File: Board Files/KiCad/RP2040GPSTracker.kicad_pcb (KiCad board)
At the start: 2 copper layers, 99.6 x 53 mm, 116 parts, among them J1 BOOTSEL, J10 GNSS, J2 RESET, J3 DEBUG, J4 BT(LE), J5 GSM, J6 USBC_CHARGE, J7 USBC_PROG, J8 2822541-1, J9 BATTERY, U1 W25Q128JVS, U10 LM66200DRLR, U2 SIM868, U3 RP2040, U4 SN74LVC1G66DRYR, U5 LM66200DRLR, U6 MP2624GL, U7 NCP1117LPST33T3G, U8 SAFFB1G56KB0F5F, Y1 Crystal

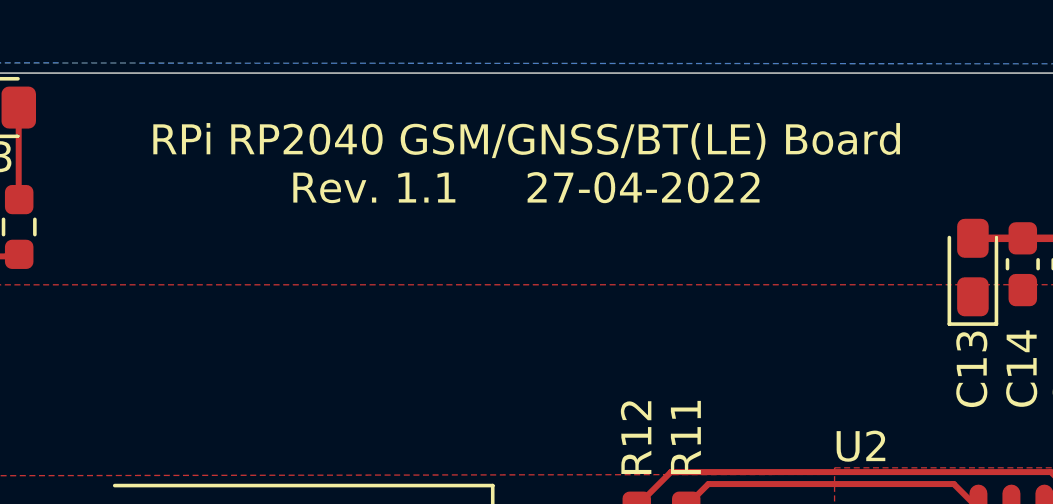
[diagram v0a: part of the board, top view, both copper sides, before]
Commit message: Updated type in Board Files
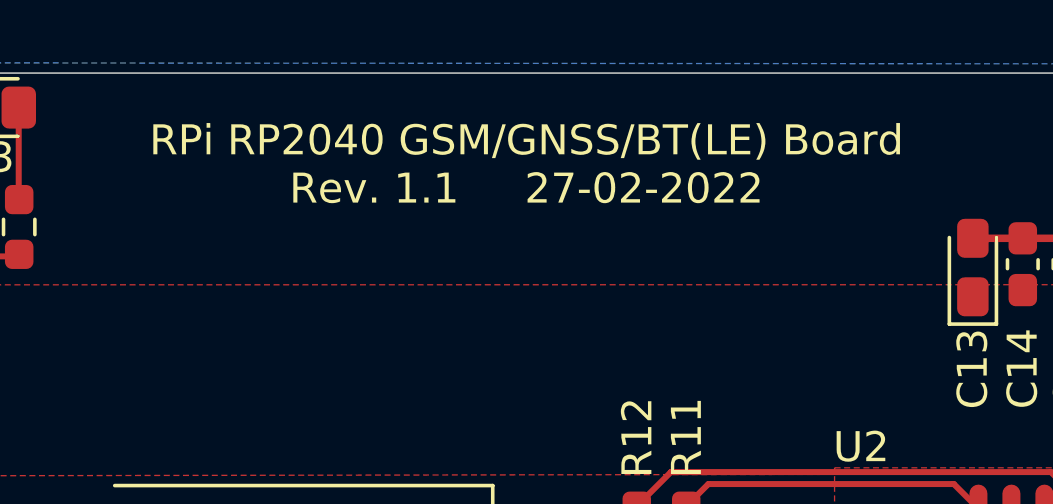
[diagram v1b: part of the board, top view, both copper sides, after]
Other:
- board text added: "RPi RP2040 GSM/GNSS/BT(LE) Board Rev. 1.1 27-02-2022"
- board text removed: "RPi RP2040 GSM/GNSS/BT(LE) Board Rev. 1.1 27-04-2022"
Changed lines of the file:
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@@
     (effects (font (size 1.5 1.5) (thickness 0.3)))
   )
-  (gr_text "RPi RP2040 GSM/GNSS/BT(LE) Board\nRev. 1.1     27-04-2022" (at 131.2852 6.9146) (layer "F.SilkS")
+  (gr_text "RPi RP2040 GSM/GNSS/BT(LE) Board\nRev. 1.1     27-02-2022" (at 131.2852 6.9146) (layer "F.SilkS")
     (effects (font (size 1 1) (thickness 0.2)))
   )

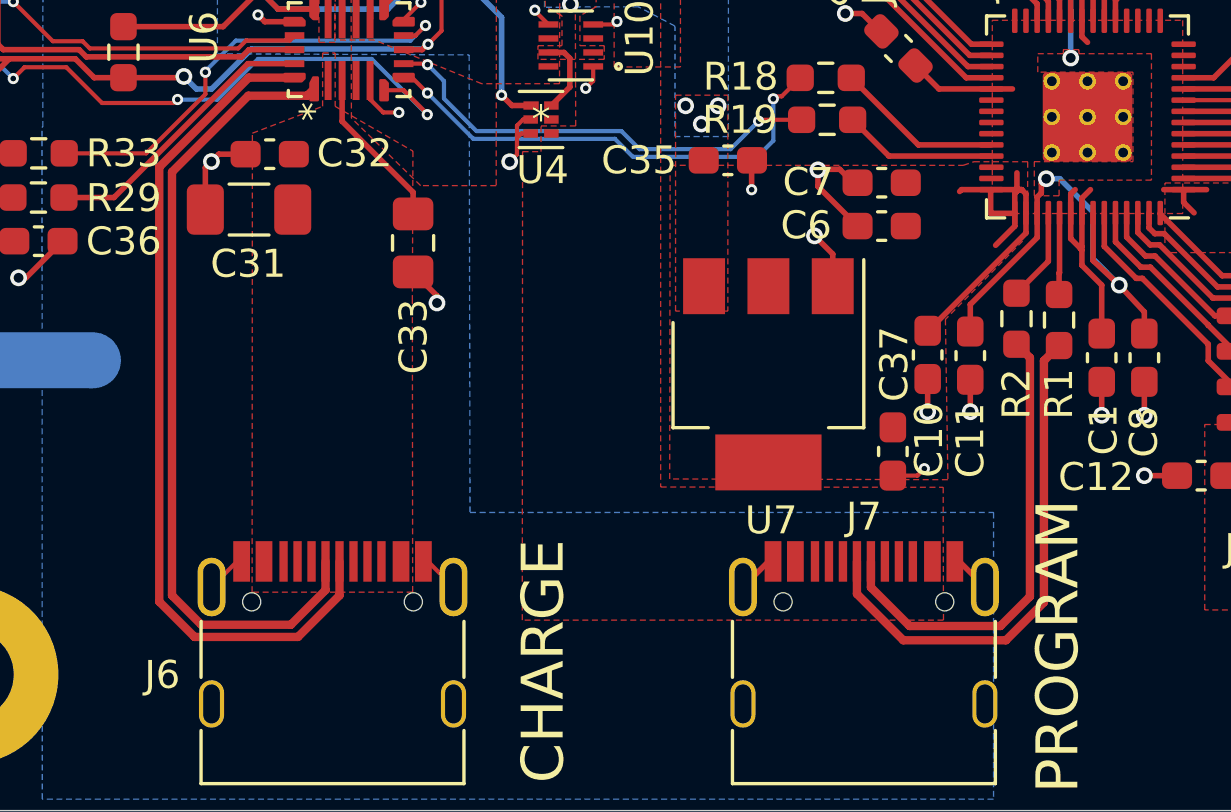
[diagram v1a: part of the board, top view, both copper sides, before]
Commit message: Updated USB trace differential routing
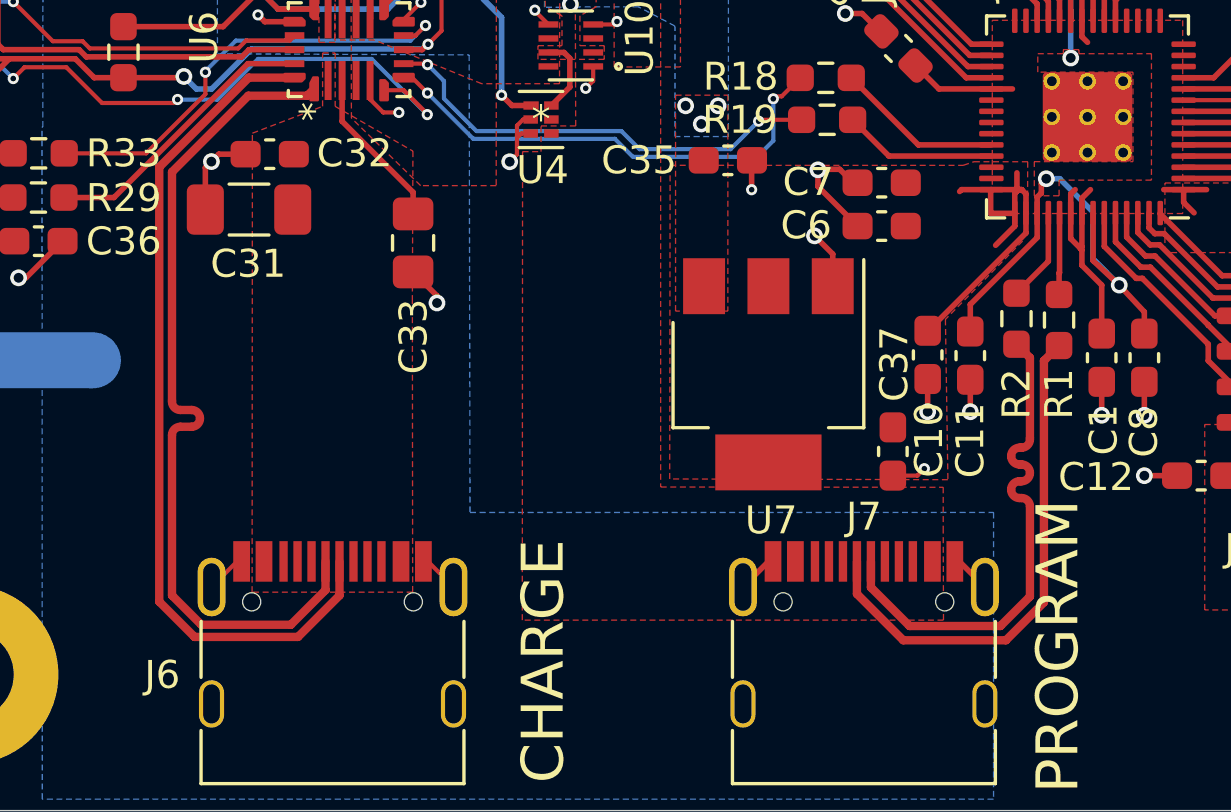
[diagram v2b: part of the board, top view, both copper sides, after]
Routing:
- net /USB_D-: track 16.8 -> 18.4 mm
- net /BCM_D+: track 28.9 -> 30.4 mm
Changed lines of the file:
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@@
 (kicad_pcb (version 20211014) (generator pcbnew)
   (general
-    (thickness 1.6)
+    (thickness 1)
   )
   (paper "A4")
@@
       (layer "F.Mask" (type "Top Solder Mask") (color "Black") (thickness 0.01))
       (layer "F.Cu" (type "copper") (thickness 0.035))
-      (layer "dielectric 1" (type "core") (thickness 1.51) (material "FR4") (epsilon_r 4.5) (loss_tangent 0.02))
+      (layer "dielectric 1" (type "core") (thickness 0.91) (material "FR4") (epsilon_r 4.5) (loss_tangent 0.02))
       (layer "B.Cu" (type "copper") (thickness 0.035))
       (layer "B.Mask" (type "Bottom Solder Mask") (color "Black") (thickness 0.01))
@@
   (segment (start 92.8852 27.3446) (end 94.0452 28.5046) (width 0.2) (layer "B.Cu") (net 33))
   (segment (start 86.053304 28.207704) (end 89.982096 28.207704) (width 0.2) (layer "B.Cu") (net 33))
-  (segment (start 113.435719 49.416911) (end 112.07803 50.7746) (width 0.3) (layer "F.Cu") (net 34))
-  (segment (start 113.9782 40.237) (end 113.43572 40.77948) (width 0.3) (layer "F.Cu") (net 34))
-  (segment (start 108.4072 50.7746) (end 106.75 49.1174) (width 0.3) (layer "F.Cu") (net 34))
-  (segment (start 112.07803 50.7746) (end 108.4072 50.7746) (width 0.3) (layer "F.Cu") (net 34))
-  (segment (start 113.43572 40.77948) (end 113.435719 49.416911) (width 0.3) (layer "F.Cu") (net 34))
-  (segment (start 106.75 49.1174) (end 106.75 47.955) (width 0.3) (layer "F.Cu") (net 34))
+  (segment (start 106.75 49.1174) (end 108.4072 50.7746) (width 0.3) (layer "F.Cu") (net 34))
+  (segment (start 108.4072 50.7746) (end 112.07803 50.7746) (width 0.3) (layer "F.Cu") (net 34))
+  (segment (start 113.43572 40.77948) (end 113.9782 40.237) (width 0.3) (layer "F.Cu") (net 34))
+  (segment (start 113.435719 49.416911) (end 113.43572 40.77948) (width 0.3) (layer "F.Cu") (net 34))
+  (segment (start 112.07803 50.7746) (end 113.435719 49.416911) (width 0.3) (layer "F.Cu") (net 34))
+  (segment (start 106.75 47.955) (end 106.75 49.1174) (width 0.3) (layer "F.Cu") (net 34))
   (segment (start 113.9782 38.412) (end 113.9782 37.647307) (width 0.2) (layer "F.Cu") (net 35))
   (segment (start 113.9782 37.647307) (end 113.9942 37.631307) (width 0.2) (layer "F.Cu") (net 35))
   (segment (start 113.9942 37.631307) (end 113.9942 35.4995) (width 0.2) (layer "F.Cu") (net 35))
-  (segment (start 112.9362 40.672) (end 112.9362 49.210002) (width 0.3) (layer "F.Cu") (net 36))
-  (segment (start 111.881602 50.2646) (end 108.631578 50.2646) (width 0.3) (layer "F.Cu") (net 36))
-  (segment (start 107.25 48.883022) (end 107.25 47.955) (width 0.3) (layer "F.Cu") (net 36))
-  (segment (start 112.4542 40.19) (end 112.9362 40.672) (width 0.3) (layer "F.Cu") (net 36))
-  (segment (start 112.9362 49.210002) (end 111.881602 50.2646) (width 0.3) (layer "F.Cu") (net 36))
-  (segment (start 108.631578 50.2646) (end 107.25 48.883022) (width 0.3) (layer "F.Cu") (net 36))
+  (segment (start 112.9362 40.672) (end 112.4542 40.19) (width 0.3) (layer "F.Cu") (net 36))
+  (segment (start 112.564043 45.0886) (end 112.6362 45.0886) (width 0.3) (layer "F.Cu") (net 36))
+  (segment (start 112.564043 43.8886) (end 112.6362 43.8886) (width 0.3) (layer "F.Cu") (net 36))
+  (segment (start 112.6362 45.6886) (end 112.564043 45.6886) (width 0.3) (layer "F.Cu") (net 36))
+  (segment (start 107.25 47.955) (end 107.25 48.883022) (width 0.3) (layer "F.Cu") (net 36))
+  (segment (start 107.25 48.883022) (end 108.631578 50.2646) (width 0.3) (layer "F.Cu") (net 36))
+  (segment (start 112.9362 43.5886) (end 112.9362 43.5386) (width 0.3) (layer "F.Cu") (net 36))
+  (segment (start 111.881602 50.2646) (end 112.9362 49.210002) (width 0.3) (layer "F.Cu") (net 36))
+  (segment (start 108.631578 50.2646) (end 111.881602 50.2646) (width 0.3) (layer "F.Cu") (net 36))
+  (segment (start 112.9362 43.5386) (end 112.9362 40.672) (width 0.3) (layer "F.Cu") (net 36))
+  (segment (start 112.9362 49.210002) (end 112.9362 45.9886) (width 0.3) (layer "F.Cu") (net 36))
+  (segment (start 112.6362 44.4886) (end 112.564043 44.4886) (width 0.3) (layer "F.Cu") (net 36))
+  (arc (start 112.6362 43.8886) (mid 112.848332 43.800732) (end 112.9362 43.5886) (width 0.3) (layer "F.Cu") (net 36))
+  (arc (start 112.9362 45.9886) (mid 112.848332 45.776468) (end 112.6362 45.6886) (width 0.3) (layer "F.Cu") (net 36))
+  (arc (start 112.9362 44.7886) (mid 112.848332 44.576468) (end 112.6362 44.4886) (width 0.3) (layer "F.Cu") (net 36))
+  (arc (start 112.264043 44.1886) (mid 112.351911 43.976468) (end 112.564043 43.8886) (width 0.3) (layer "F.Cu") (net 36))
+  (arc (start 112.264043 45.3886) (mid 112.351911 45.176468) (end 112.564043 45.0886) (width 0.3) (layer "F.Cu") (net 36))
+  (arc (start 112.6362 45.0886) (mid 112.848332 45.000732) (end 112.9362 44.7886) (width 0.3) (layer "F.Cu") (net 36))
+  (arc (start 112.564043 45.6886) (mid 112.351911 45.600732) (end 112.264043 45.3886) (width 0.3) (layer "F.Cu") (net 36))
+  (arc (start 112.564043 44.4886) (mid 112.351911 44.400732) (end 112.264043 44.1886) (width 0.3) (layer "F.Cu") (net 36))
   (segment (start 112.4542 38.365) (end 113.5942 37.225) (width 0.2) (layer "F.Cu") (net 37))
   (segment (start 113.5942 37.225) (end 113.5942 35.4995) (width 0.2) (layer "F.Cu") (net 37))
@@
   (segment (start 154.94 19.5834) (end 160.3725 19.5834) (width 0.2) (layer "F.Cu") (net 106))
   (segment (start 160.3725 19.5834) (end 160.4313 19.5246) (width 0.2) (layer "F.Cu") (net 106))
-  (segment (start 82.2612 49.1706) (end 82.2612 34.03179) (width 0.3) (layer "F.Cu") (net 124))
-  (segment (start 84.98839 31.3046) (end 87.095559 31.3046) (width 0.3) (layer "F.Cu") (net 124))
-  (segment (start 87.095559 31.3046) (end 87.342455 31.057704) (width 0.3) (layer "F.Cu") (net 124))
-  (segment (start 87.75 47.955) (end 87.75 48.98) (width 0.3) (layer "F.Cu") (net 124))
+  (segment (start 82.2612 42.2406) (end 82.2612 42.1906) (width 0.3) (layer "F.Cu") (net 124))
+  (segment (start 82.2612 34.03179) (end 84.98839 31.3046) (width 0.3) (layer "F.Cu") (net 124))
   (segment (start 83.31012 50.21952) (end 82.2612 49.1706) (width 0.3) (layer "F.Cu") (net 124))
+  (segment (start 87.095559 31.3046) (end 87.342455 31.057704) (width 0.3) (layer "F.Cu") (net 124))
+  (segment (start 82.9612 42.5406) (end 82.5612 42.5406) (width 0.3) (layer "F.Cu") (net 124))
+  (segment (start 84.98839 31.3046) (end 87.095559 31.3046) (width 0.3) (layer "F.Cu") (net 124))
   (segment (start 87.75 48.98) (end 86.51048 50.21952) (width 0.3) (layer "F.Cu") (net 124))
+  (segment (start 82.2612 49.1706) (end 82.2612 43.4406) (width 0.3) (layer "F.Cu") (net 124))
+  (segment (start 82.2612 42.1906) (end 82.2612 34.03179) (width 0.3) (layer "F.Cu") (net 124))
+  (segment (start 82.5612 43.1406) (end 82.9612 43.1406) (width 0.3) (layer "F.Cu") (net 124))
+  (segment (start 87.75 47.955) (end 87.75 48.98) (width 0.3) (layer "F.Cu") (net 124))
   (segment (start 86.51048 50.21952) (end 83.31012 50.21952) (width 0.3) (layer "F.Cu") (net 124))
-  (segment (start 82.2612 34.03179) (end 84.98839 31.3046) (width 0.3) (layer "F.Cu") (net 124))
+  (arc (start 82.5612 42.5406) (mid 82.349068 42.452732) (end 82.2612 42.2406) (width 0.3) (layer "F.Cu") (net 124))
+  (arc (start 82.2612 43.4406) (mid 82.349068 43.228468) (end 82.5612 43.1406) (width 0.3) (layer "F.Cu") (net 124))
+  (arc (start 82.9612 43.1406) (mid 83.173332 43.052732) (end 83.2612 42.8406) (width 0.3) (layer "F.Cu") (net 124))
+  (arc (start 83.2612 42.8406) (mid 83.173332 42.628468) (end 82.9612 42.5406) (width 0.3) (layer "F.Cu") (net 124))
   (segment (start 86.767111 50.6546) (end 83.0652 50.6546) (width 0.3) (layer "F.Cu") (net 125))
   (segment (start 81.8052 33.8581) (end 85.005344 30.657956) (width 0.3) (layer "F.Cu") (net 125))

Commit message: Board optimizations
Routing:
- net Net-(C28-Pad2): track 34.5 -> 31.3 mm
- net Net-(C30-Pad2): track 36.0 -> 37.0 mm

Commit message: Rev 1.2, Swapped out C13 Footprint for more suitable one
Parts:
- C13: footprint Capacitor_Tantalum_SMD:CP_EIA-2012-15_AVX-P_Pad1.30x1.05mm_HandSolder -> Capacitor_Tantalum_SMD:CP_EIA-3528-15_AVX-H
- moved C13 1.25 mm to (145.3, 9.44)
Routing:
- net GND: track 123.7 -> 125.2 mm
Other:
- board text added: "Board Rev.: 1.2 16-03-2022"
- board text added: "RPi RP2040 GSM/GNSS/BT(LE) Board Model: RP2040-868 - justSem.org"
- board text removed: "Board Rev.: 1.1 27-02-2022"
- board text removed: "RPi RP2040 GSM/GNSS/BT(LE) Board Rev. 1.1 27-02-2022"
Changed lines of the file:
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@@
     (fp_line (start -0.254724 -0.5225) (end 0.254724 -0.5225) (layer "F.SilkS") (width 0.12))
     (fp_line (start 1.65 0.73) (end -1.65 0.73) (layer "F.CrtYd") (width 0.05))
-    (fp_line (start -1.65 0.73) (end -1.65 -0.73) (layer "F.CrtYd") (width 0.05))
-    (fp_line (start 1.65 -0.73) (end 1.65 0.73) (layer "F.CrtYd") (width 0.05))
     (fp_line (start -1.65 -0.73) (end 1.65 -0.73) (layer "F.CrtYd") (width 0.05))
+    (fp_line (start 1.65 -0.73) (end 1.65 0.73) (layer "F.CrtYd") (width 0.05))
+    (fp_line (start -1.65 0.73) (end -1.65 -0.73) (layer "F.CrtYd") (width 0.05))
     (fp_line (start 0.8 -0.4125) (end 0.8 0.4125) (layer "F.Fab") (width 0.1))
     (fp_line (start -0.8 -0.4125) (end 0.8 -0.4125) (layer "F.Fab") (width 0.1))
@@
     )
   )
-  (footprint "Capacitor_Tantalum_SMD:CP_EIA-2012-15_AVX-P_Pad1.30x1.05mm_HandSolder" (layer "F.Cu")
-    (at 146.1652 10.3476 90)
-    (descr "Tantalum Capacitor SMD AVX-P (2012-15 Metric), IPC_7351 nominal, (Body size from: https://www.vishay.com/docs/40182/tmch.pdf), generated with kicad-footprint-generator")
+  (footprint "Capacitor_Tantalum_SMD:CP_EIA-3528-15_AVX-H" (layer "F.Cu")
+    (at 145.3052 9.4421 90)
+    (descr "Tantalum Capacitor SMD AVX-H (3528-15 Metric), IPC_7351 nominal, (Body size from: http://www.kemet.com/Lists/ProductCatalog/Attachments/253/KEM_TC101_STD.pdf), generated with kicad-footprint-generator")
     (tags "capacitor tantalum")
     (property "Sheetfile" "RP2040GPSTracker.kicad_sch")
     (property "Sheetname" "")
     (attr smd)
-    (fp_text reference "C13" (at -3.375 0 90) (layer "F.SilkS")
+    (fp_text reference "C13" (at 0 -2.35 90) (layer "F.SilkS")
       (effects (font (size 1 1) (thickness 0.15)))
     )
-    (fp_text value "100uF" (at 0 1.58 90) (layer "F.Fab")
+    (fp_text value "100uF" (at 0 2.35 90) (layer "F.Fab")
       (effects (font (size 1 1) (thickness 0.15)))
     )
     (fp_text user "${REFERENCE}" (at 0 0 90) (layer "F.Fab")
-      (effects (font (size 0.5 0.5) (thickness 0.08)))
+      (effects (font (size 0.88 0.88) (thickness 0.13)))
     )
-    (fp_line (start -1.885 0.785) (end 1 0.785) (layer "F.SilkS") (width 0.12))
-    (fp_line (start 1 -0.785) (end -1.885 -0.785) (layer "F.SilkS") (width 0.12))
-    (fp_line (start -1.885 -0.785) (end -1.885 0.785) (layer "F.SilkS") (width 0.12))
-    (fp_line (start -1.88 -0.88) (end 1.88 -0.88) (layer "F.CrtYd") (width 0.05))
-    (fp_line (start 1.88 0.88) (end -1.88 0.88) (layer "F.CrtYd") (width 0.05))
-    (fp_line (start -1.88 0.88) (end -1.88 -0.88) (layer "F.CrtYd") (width 0.05))
-    (fp_line (start 1.88 -0.88) (end 1.88 0.88) (layer "F.CrtYd") (width 0.05))
-    (fp_line (start -1 -0.3125) (end -1 0.625) (layer "F.Fab") (width 0.1))
-    (fp_line (start 1 0.625) (end 1 -0.625) (layer "F.Fab") (width 0.1))
-    (fp_line (start -1 0.625) (end 1 0.625) (layer "F.Fab") (width 0.1))
-    (fp_line (start -0.6875 -0.625) (end -1 -0.3125) (layer "F.Fab") (width 0.1))
-    (fp_line (start 1 -0.625) (end -0.6875 -0.625) (layer "F.Fab") (width 0.1))
-    (pad "1" smd roundrect (at -0.975 0 90) (size 1.3 1.05) (layers "F.Cu" "F.Paste" "F.Mask") (roundrect_rratio 0.2380952381)
+    (fp_line (start -2.46 1.51) (end 1.75 1.51) (layer "F.SilkS") (width 0.12))
+    (fp_line (start 1.75 -1.51) (end -2.46 -1.51) (layer "F.SilkS") (width 0.12))
+    (fp_line (start -2.46 -1.51) (end -2.46 1.51) (layer "F.SilkS") (width 0.12))
+    (fp_line (start 2.45 1.65) (end -2.45 1.65) (layer "F.CrtYd") (width 0.05))
+    (fp_line (start 2.45 -1.65) (end 2.45 1.65) (layer "F.CrtYd") (width 0.05))
+    (fp_line (start -2.45 -1.65) (end 2.45 -1.65) (layer "F.CrtYd") (width 0.05))
+    (fp_line (start -2.45 1.65) (end -2.45 -1.65) (layer "F.CrtYd") (width 0.05))
+    (fp_line (start -1.75 -0.7) (end -1.75 1.4) (layer "F.Fab") (width 0.1))
+    (fp_line (start -1.75 1.4) (end 1.75 1.4) (layer "F.Fab") (width 0.1))
+    (fp_line (start -1.05 -1.4) (end -1.75 -0.7) (layer "F.Fab") (width 0.1))
+    (fp_line (start 1.75 -1.4) (end -1.05 -1.4) (layer "F.Fab") (width 0.1))
+    (fp_line (start 1.75 1.4) (end 1.75 -1.4) (layer "F.Fab") (width 0.1))
+    (pad "1" smd roundrect (at -1.5375 0 90) (size 1.325 2.35) (layers "F.Cu" "F.Paste" "F.Mask") (roundrect_rratio 0.1886792453)
       (net 4 "/SIM_PWR") (pintype "passive"))
-    (pad "2" smd roundrect (at 0.975 0 90) (size 1.3 1.05) (layers "F.Cu" "F.Paste" "F.Mask") (roundrect_rratio 0.2380952381)
+    (pad "2" smd roundrect (at 1.5375 0 90) (size 1.325 2.35) (layers "F.Cu" "F.Paste" "F.Mask") (roundrect_rratio 0.1886792453)
       (net 1 "GND") (pintype "passive"))
-    (model "${KICAD6_3DMODEL_DIR}/Capacitor_Tantalum_SMD.3dshapes/CP_EIA-2012-15_AVX-P.wrl"
+    (model "${KICAD6_3DMODEL_DIR}/Capacitor_Tantalum_SMD.3dshapes/CP_EIA-3528-15_AVX-H.wrl"
       (offset (xyz 0 0 0))
       (scale (xyz 1 1 1))
@@
     (effects (font (size 1 1) (thickness 0.15)) (justify mirror))
   )
-  (gr_text "Board Rev.: 1.1     27-02-2022" (at 144.2952 54.9846) (layer "B.SilkS")
+  (gr_text "Board Rev.: 1.2     16-03-2022" (at 144.2952 54.9846) (layer "B.SilkS")
     (effects (font (size 1.5 1.5) (thickness 0.3)) (justify mirror))
   )
@@
     (effects (font (size 1.5 1.5) (thickness 0.3)))
   )
-  (gr_text "RPi RP2040 GSM/GNSS/BT(LE) Board\nRev. 1.1     27-02-2022" (at 131.2852 6.9146) (layer "F.SilkS")
-    (effects (font (size 1 1) (thickness 0.2)))
+  (gr_text "RPi RP2040 GSM/GNSS/BT(LE) Board\nModel: RP2040-868 - justSem.org" (at 115.7852 6.5396) (layer "F.SilkS")
+    (effects (font (size 1 1) (thickness 0.2)) (justify left))
   )
   (gr_text "Batch: #JLCJLCJLCJLC" (at 126.4352 55.9646) (layer "F.SilkS")
@@
   )
   (segment (start 94.755201 32.654599) (end 94.5952 32.8146) (width 0.15) (layer "F.Cu") (net 1))
+  (segment (start 146.773 9.3724) (end 152.908 9.3724) (width 0.25) (layer "F.Cu") (net 1))
   (segment (start 116.4336 27.4574) (end 116.7384 27.4574) (width 0.2) (layer "F.Cu") (net 1))
   (segment (start 108.5052 5.0046) (end 108.5052 6.0446) (width 0.15) (layer "F.Cu") (net 1))
-  (segment (start 146.1654 9.3724) (end 152.908 9.3724) (width 0.25) (layer "F.Cu") (net 1))
   (segment (start 139.5752 50.44386) (end 140.2552 51.12386) (width 0.2) (layer "F.Cu") (net 1))
   (segment (start 72.4602 27.1646) (end 72.6052 27.3096) (width 0.15) (layer "F.Cu") (net 1))
@@
   (segment (start 104.7102 6.2146) (end 104.4852 6.4396) (width 0.15) (layer "F.Cu") (net 1))
   (segment (start 143.2102 40.6551) (end 143.2102 41.1996) (width 0.2) (layer "F.Cu") (net 1))
+  (segment (start 145.3052 7.9046) (end 146.773 9.3724) (width 0.25) (layer "F.Cu") (net 1))
   (segment (start 156.8777 15.6246) (end 156.8777 14.0746) (width 0.25) (layer "F.Cu") (net 1))
   (segment (start 100.8902 5.0046) (end 100.8902 6.2096) (width 0.15) (layer "F.Cu") (net 1))
@@
   (segment (start 137.1852 38.3146) (end 138.3052 38.3146) (width 0.2) (layer "F.Cu") (net 1))
   (segment (start 160.0552 47.5846) (end 160.0552 46.3771) (width 0.2) (layer "F.Cu") (net 1))
-  (segment (start 146.1652 9.3726) (end 146.1654 9.3724) (width 0.25) (layer "F.Cu") (net 1))
   (segment (start 168.0052 19.8246) (end 168.0052 20.8446) (width 0.2) (layer "F.Cu") (net 1))
   (segment (start 132.226 28.1656) (end 131.17704 28.1656) (width 0.2) (layer "F.Cu") (net 1))
